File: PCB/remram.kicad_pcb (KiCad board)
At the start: 4 copper layers, 140 x 103 mm, 208 parts, among them J1 4DB-P108-06, J10 70543-0002, J11 Conn_02x13_Odd_Even, J12 70543-0002, J13 70543-0002, J14 70543-0002, J15 70543-0003, J16 62201021121, J17 70543-0001, J18 70543-0001, J19 70543-0001, J2 039531-1002, J20 70543-0003, J21 70543-0003, J22 70543-0003, J23 70543-0003, J3 70543-0002, J4 70543-0002, J5 70543-0002, J6 67068-8000, J7 Conn_02x05, J8 Conn_02x05, J9 70543-0002, Q1 PSMN1R8-40YLC,115, Q2 BUK9840-55, Q3 PSMN1R8-40YLC,115, Q4 BUK9840-55, SW1 OS102011MA1QN1, SW2 PTS645VL39-2, U1 TPS54308, U2 AP2112K-3.3TRG1, U3 ADUM4160, U4 STM32F765VIT6, U5 TMC2130-TA, U6 TMC2130-TA, U7 TMC2130-TA, U8 TMC2130-TA, Y1 TSX-3225 24.0000MF15X-AC3

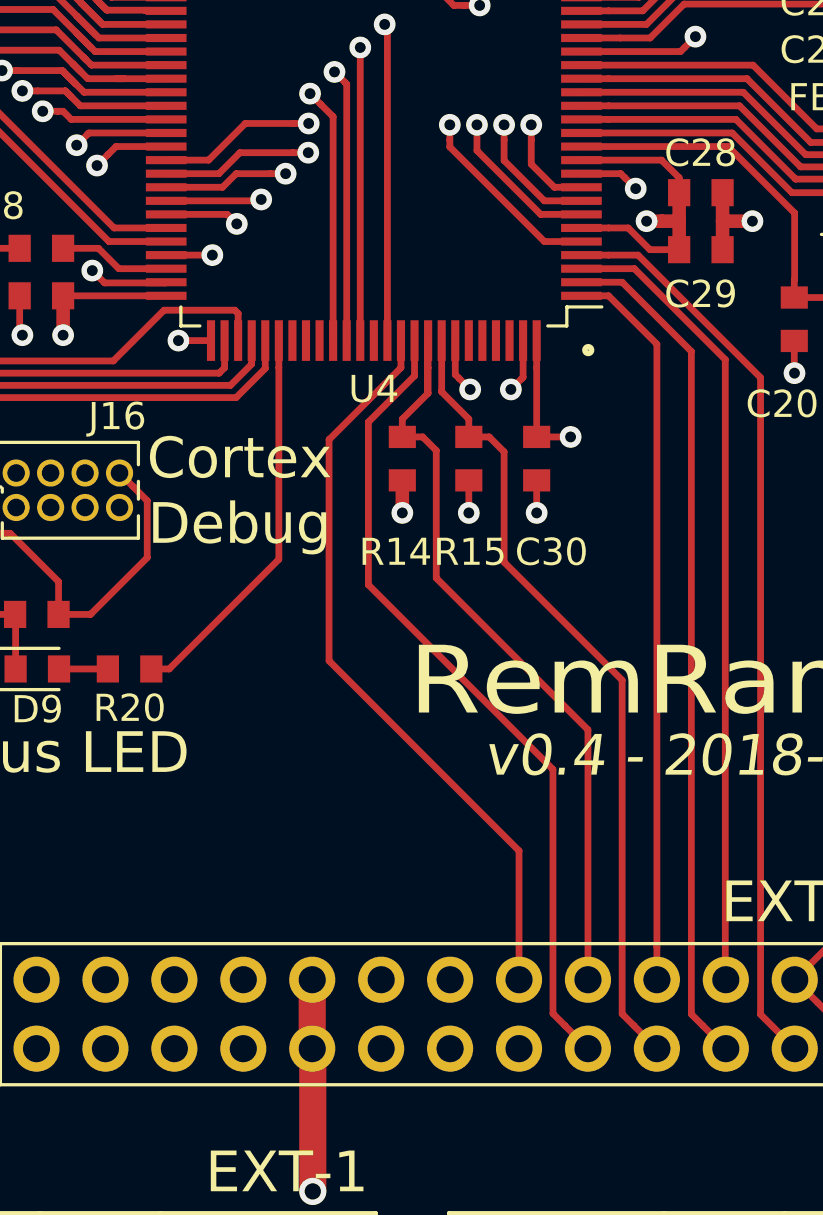
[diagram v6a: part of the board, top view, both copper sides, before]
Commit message: Removed USART1 CK pin and added another digial pin.
STM32duino doesn't seem to support USART. So I will only
implement the UART pins.
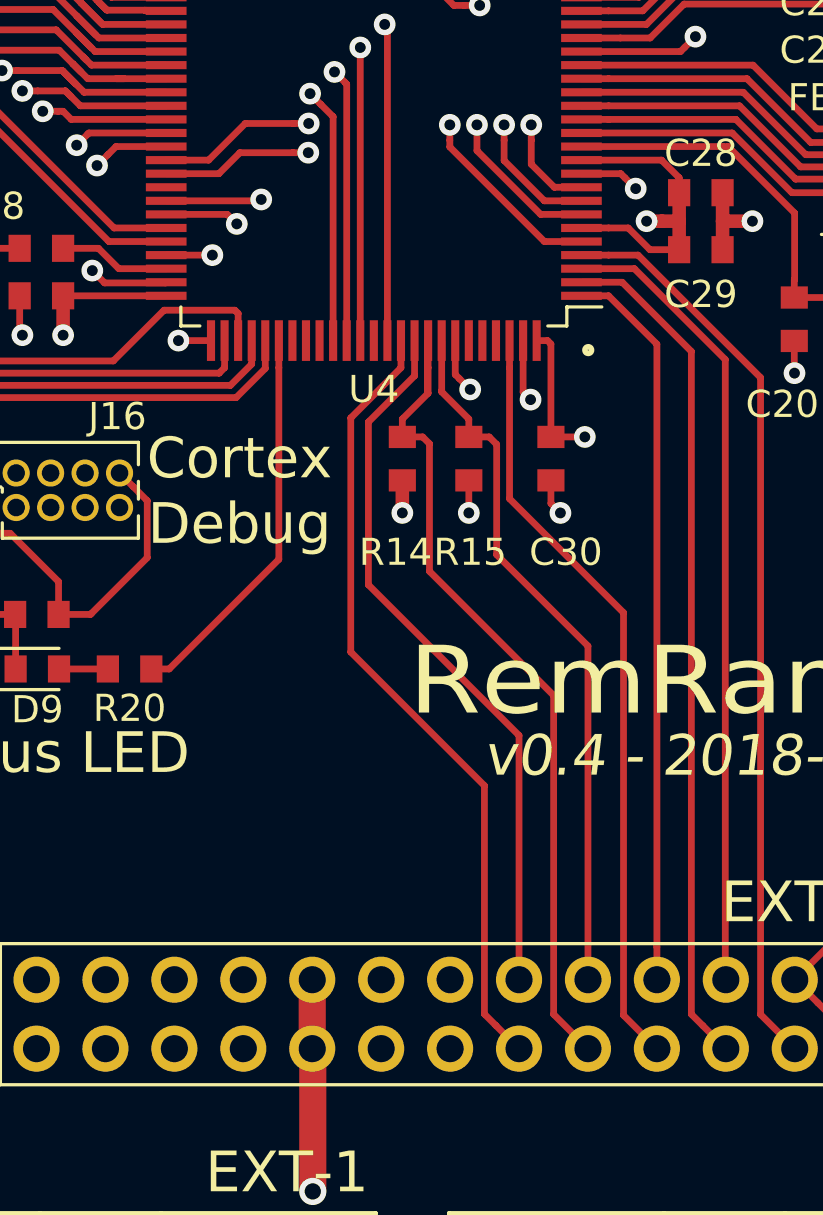
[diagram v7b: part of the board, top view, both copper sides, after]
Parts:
- moved C30 0.52 mm to (127.2, 105.0)
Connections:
- J11 pad 10: /MCU/PWM_EXT1 -> /MCU/SCL
- J11 pad 11: /MCU/PWM_EXT2 -> /MCU/PWM_EXT1
- J11 pad 12: /MCU/PWM_EXT3 -> /MCU/PWM_EXT2
- J11 pad 13: /MCU/PWM_EXT4 -> /MCU/PWM_EXT3
- J11 pad 14: /MCU/USART_CK -> /MCU/PWM_EXT4
- J11 pad 8: /MCU/SDA -> /MCU/EXT_D5
- J11 pad 9: /MCU/SCL -> /MCU/SDA
- U4 pad 67: /MCU/USART_CK -> Net-(U4-Pad67)
- U4 pad 98: Net-(U4-Pad98) -> /MCU/EXT_D5
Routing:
- net /MCU/USART_CK: track 39.4 -> 0.00 mm, vias 1 -> 0
- net /MCU/EXT_D5: track 0.00 -> 28.3 mm
- net /MCU/SDA: track 29.8 -> 26.2 mm
- net /MCU/PWM_EXT1: track 30.1 -> 26.6 mm
- net /MCU/PWM_EXT3: track 43.1 -> 39.5 mm
- net /MCU/SCL: track 29.1 -> 31.6 mm
- net /MCU/PWM_EXT4: track 38.2 -> 40.7 mm
- net /MCU/PWM_EXT2: track 27.5 -> 29.4 mm
